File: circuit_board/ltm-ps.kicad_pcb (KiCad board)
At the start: 2 copper layers, 50 x 50 mm, 26 parts, among them J1 0826-1X1T-M1-F, J2 RJHSE-5080, P1 CONN_01X02, P2 CONN_01X02, P3 CONN_01X02, U1 NCP1092, U2 LTM8050

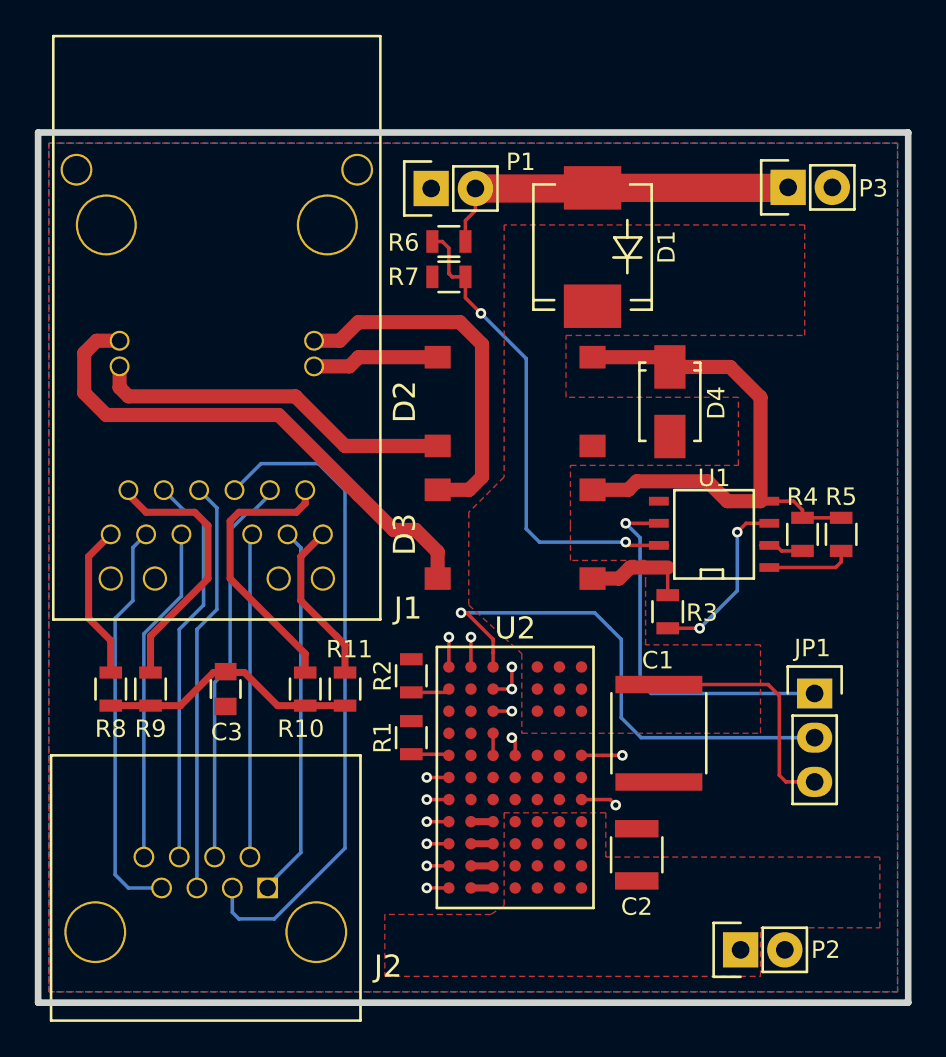
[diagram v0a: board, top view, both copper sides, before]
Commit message: review design: correct inverting RJ45 signals. Modify ltm feedback resistor from 89.4k to 90.9k. Add silkscreen text for jumper
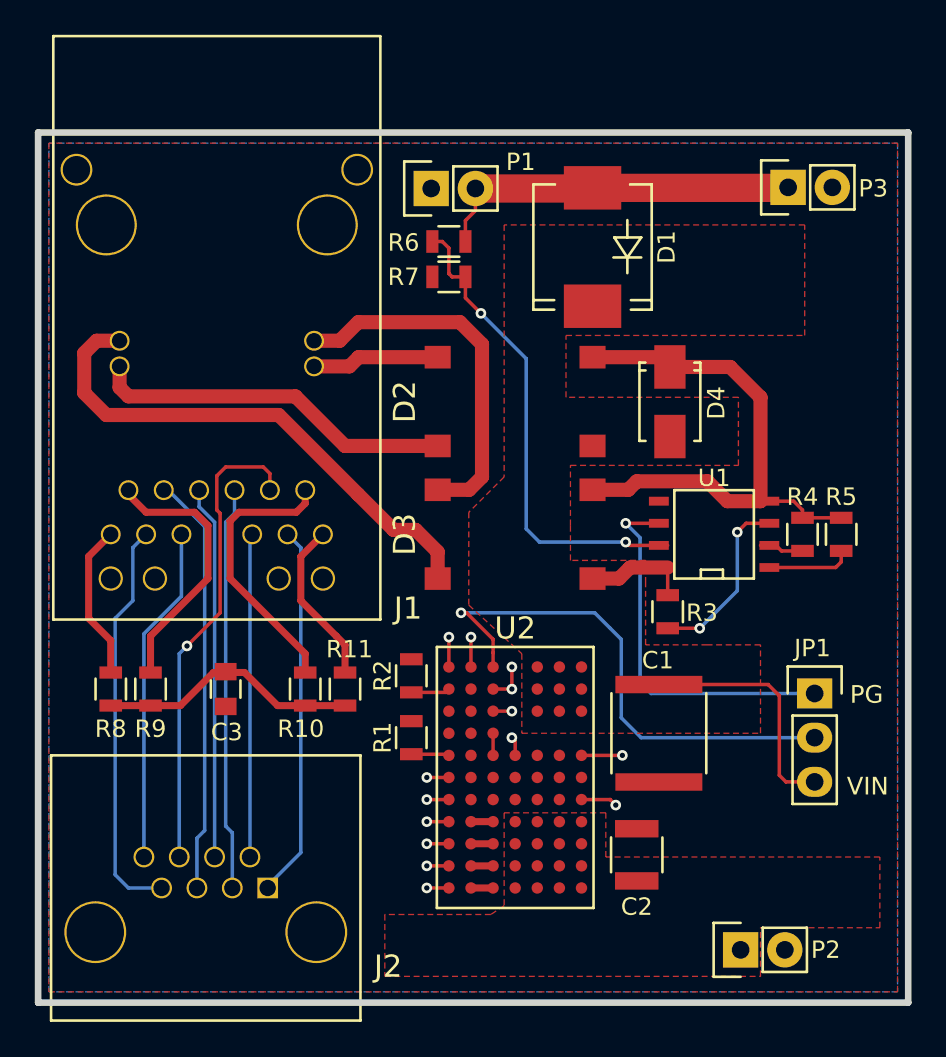
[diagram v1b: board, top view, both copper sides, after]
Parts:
- R2: value 89.4k -> 90.9k
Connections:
- J2 pad 4: /TRD2- -> /TRD3+
- J2 pad 5: /TRD3+ -> /TRD3-
- J2 pad 6: /TRD3- -> /TRD2-
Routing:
- net /TRD2+: track 37.9 -> 23.2 mm
- net /TRD2-: track 22.5 -> 27.6 mm, vias 0 -> 1
- net /TRD3+: track 23.8 -> 21.5 mm
- net /TRD3-: track 22.9 -> 24.2 mm
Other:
- board text added: "PG"
- board text added: "VIN"
